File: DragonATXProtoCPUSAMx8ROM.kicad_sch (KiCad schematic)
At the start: 22 parts, among them IC1 HD63C09, IC11 74LS08, IC25 74LS244, IC3 74LS138, IC39 6883, IC4 74LS02, U4 28C256

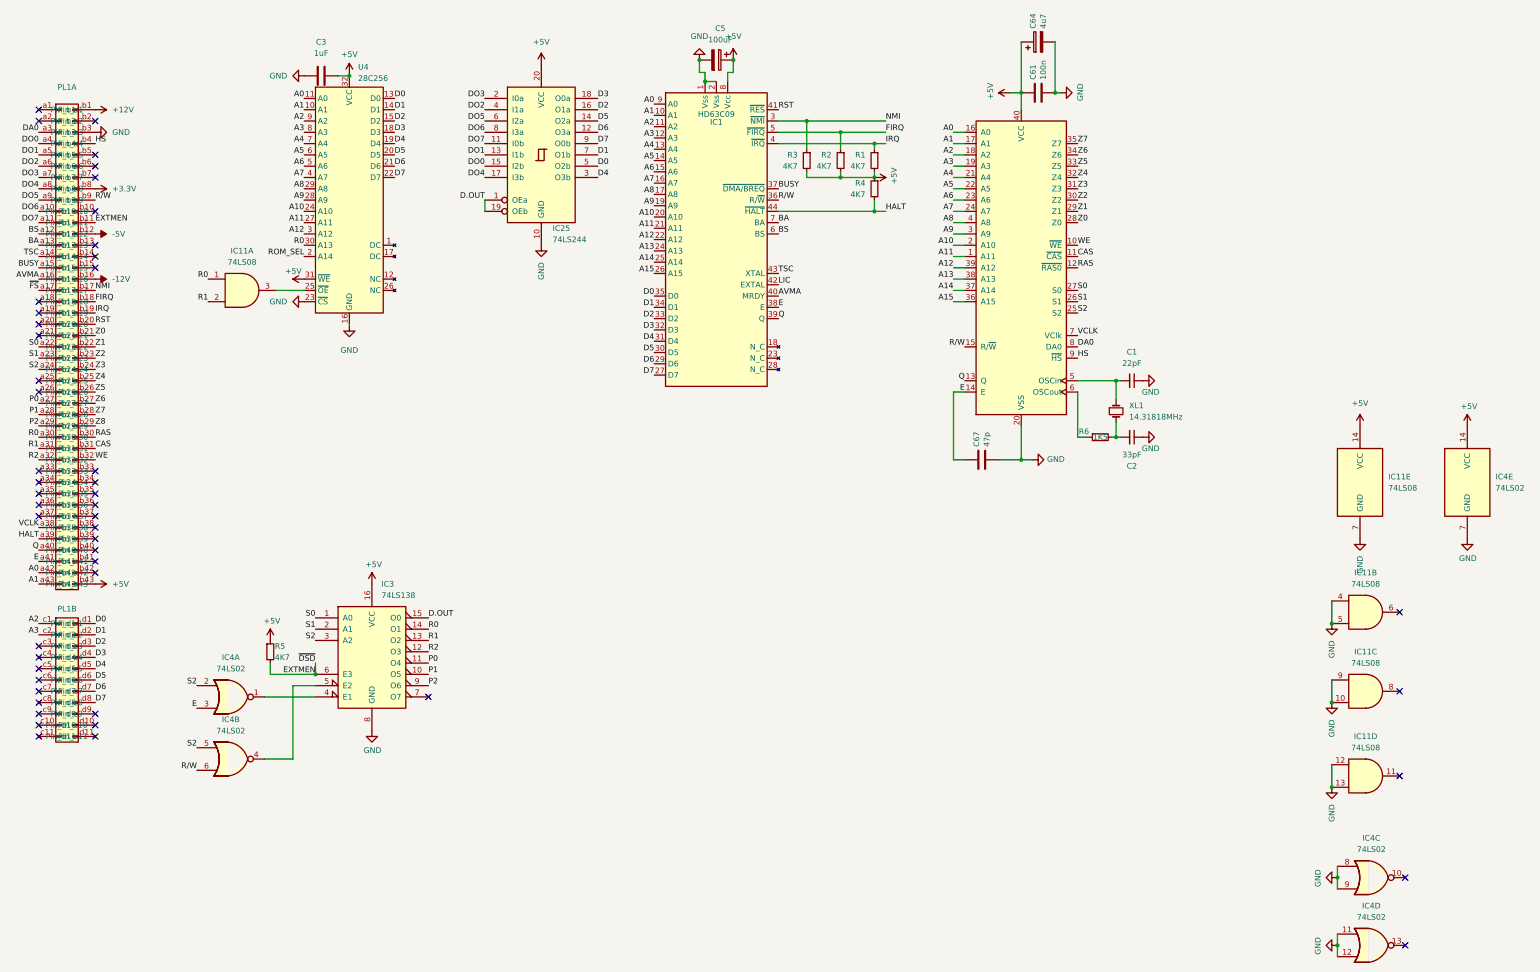
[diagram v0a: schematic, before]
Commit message: wire in upper address lines for cartridge port
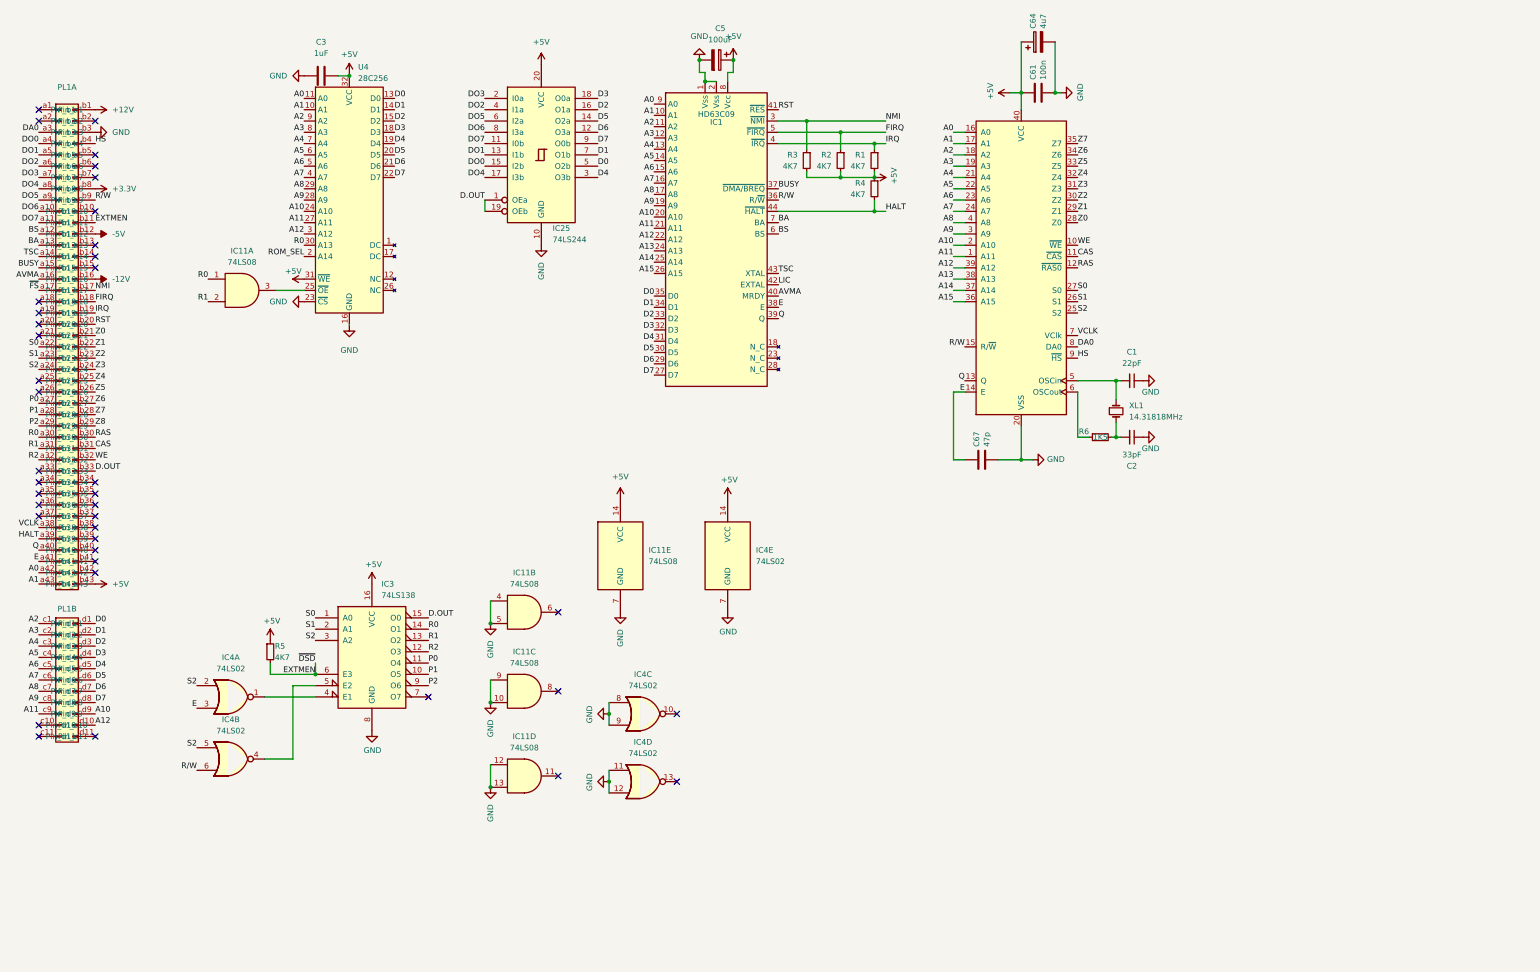
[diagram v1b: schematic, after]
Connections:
- net A10: now also PL1.d9 (Pin_d9)
- net A11: now also PL1.c9 (Pin_c9)
- net A12: now also PL1.d10 (Pin_d10)
- net A4: now also PL1.c3 (Pin_c3)
- net A5: now also PL1.c4 (Pin_c4)
- net A6: now also PL1.c5 (Pin_c5)
- net A7: now also PL1.c6 (Pin_c6)
- net A8: now also PL1.c7 (Pin_c7)
- net A9: now also PL1.c8 (Pin_c8)
- net D.OUT: now also PL1.b33 (Pin_b33)
- no-connect marks 49 -> 39
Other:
- moved on the sheet: IC11B, IC11C, IC11D, IC11E, IC4C, IC4D, IC4E
